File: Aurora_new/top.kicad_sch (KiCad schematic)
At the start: 27 parts, among them J17 Screw_Terminal_01x02, J18 Screw_Terminal_01x04, J19 TSW-104-27-G-D, J20 TSW-104-27-G-D, J21 XT60-M, J26 Screw_Terminal_01x08, J27 Screw_Terminal_01x08, J28 Screw_Terminal_01x03, J29 Screw_Terminal_01x03, J30 Screw_Terminal_01x03, J31 Screw_Terminal_01x03, J32 Screw_Terminal_01x03, J37 Screw_Terminal_01x03, J38 Screw_Terminal_01x03, J39 TSW-104-27-G-D, J40 XT60-M, U10 ADS1115IDGS, U11 ADS1115IDGS, U12 L7805, U8 ADS1115IDGS

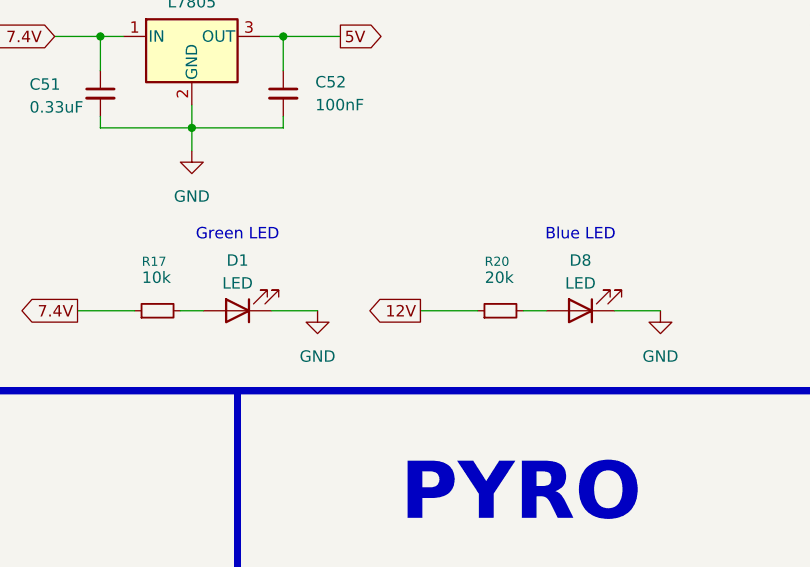
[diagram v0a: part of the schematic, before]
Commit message: bom updates (purchase links, prices, etc) and switching imu because out of stock
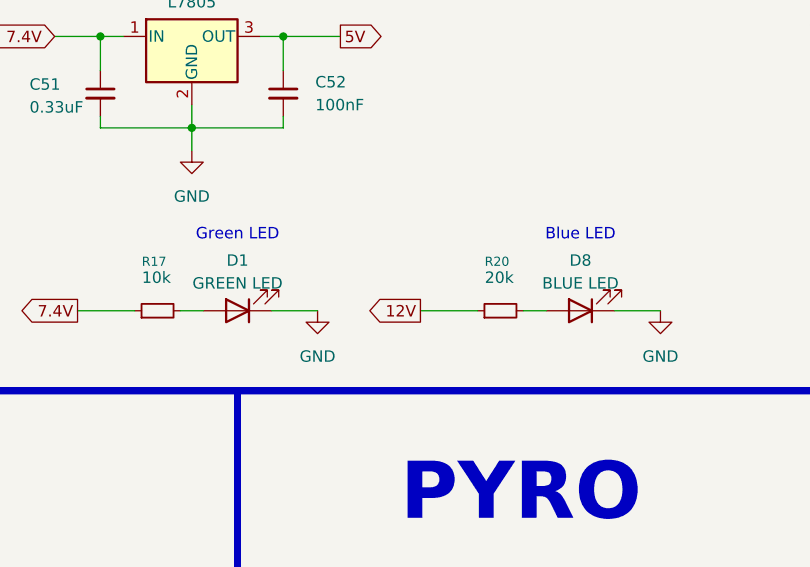
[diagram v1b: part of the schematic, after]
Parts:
- C51: PURCHASE-URL (none) -> https://www.digikey.com/en/products/detail/murata-electroni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; Price (none) -> $0.36000
- C52: PURCHASE-URL (none) -> https://www.digikey.com/en/products/detail/kyocera-avx/KGM1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; Price (none) -> $0.00700
- D1: value LED -> GREEN LED; PURCHASE-URL (none) -> https://www.digikey.com/en/products/detail/ams-osram-usa-in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; Price (none) -> $0.10200
- D8: value LED -> BLUE LED; PURCHASE-URL (none) -> https://www.digikey.com/en/products/detail/w%C3%BCrth-elekt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; Price (none) -> $0.17600
- J17: PURCHASE-URL (none) -> https://www.digikey.com/en/products/detail/phoenix-contact/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; Price (none) -> $1.33000
- J18: PURCHASE-URL (none) -> https://www.digikey.com/en/products/detail/phoenix-contact/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; Price (none) -> $2.06500
- J19, J20, J39: PURCHASE-URL (none) -> https://www.digikey.com/en/products/detail/samtec-inc/TSW-1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; Price (none) -> $1.81000
- J21, J40: PURCHASE-URL (none) -> https://www.tme.com/us/en-us/details/xt60-m/dc-power-connec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; Price (none) -> $0.602
- J26, J27: PURCHASE-URL (none) -> https://www.digikey.com/en/products/detail/phoenix-contact/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; Price (none) -> $4.07700
- J28, J29, J30, J31, J32, J37, J38: footprint (none) -> 1935174:PHOENIX_1935174; PURCHASE-URL (none) -> https://www.digikey.com/en/products/detail/phoenix-contact/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; Price (none) -> $0.74800
- R17: PURCHASE-URL (none) -> https://www.digikey.com/en/products/detail/bourns-inc/CR080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; Price (none) -> $0.00442
- R20: PURCHASE-URL (none) -> https://www.digikey.com/en/products/detail/bourns-inc/CR080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; Price (none) -> $0.00544
- U10, U11, U8: PURCHASE-URL (none) -> https://www.digikey.com/en/products/detail/texas-instrument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; Price (none) -> $5.12000
- U12: PURCHASE-URL (none) -> https://www.digikey.com/en/products/detail/stmicroelectroni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; Price (none) -> $0.50000

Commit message: added pyros, voltage booster
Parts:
- removed C51: 0.33uF, Capacitor_SMD:C_0805_2012Metric, symbol Device:C_Small
- removed C52: 100nF, Capacitor_SMD:C_0805_2012Metric, symbol Device:C_Small
- removed D8: BLUE LED, LED_SMD:LED_Cree-PLCC4_5x5mm_CW, symbol Device:LED
- removed J40: XT60-M, XT60-M:AMASS_XT60-M, symbol XT60-M:XT60-M
- removed U12: L7805, L7805:TO255P1020X450X2000-3, symbol Regulator_Linear:L7805
- added C62, C68: 22uf, Capacitor_SMD:C_0805_2012Metric, symbol Device:C_Small
- added C63, C67: 100nf, Capacitor_SMD:C_0805_2012Metric, symbol Device:C_Small
- added C64: 4.7uf, Capacitor_SMD:C_0805_2012Metric, symbol Device:C_Small
- added C65: 47pf, Capacitor_SMD:C_0805_2012Metric, symbol Device:C_Small
- added C66: 680pf, Capacitor_SMD:C_0805_2012Metric, symbol Device:C_Small
- added C69: 10uF, Capacitor_SMD:C_0805_2012Metric, symbol Device:C_Small
- added C70: 1uF, Capacitor_SMD:C_0805_2012Metric, symbol Device:C_Small
- added C71: 47uF, Capacitor_SMD:C_0805_2012Metric, symbol Device:C_Small
- added D6, D8: 1N4148W, Diode_SMD:D_SOD-123, symbol Diode:1N4148W
- added J40: Screw_Terminal_01x03, 1935174:PHOENIX_1935174, symbol Connector:Screw_Terminal_01x03
- added J42, J43: Screw_Terminal_01x04, footprints6:CONN_1715747_PXC, symbol Connector:Screw_Terminal_01x04
- added J44, J45, J46: Screw_Terminal_01x02, footprints5:CONN_1729128_PXC, symbol Connector:Screw_Terminal_01x02
- added L1: 2.2uH, symbol Device:L
- added Q1, Q2, Q5, Q6: AO3400A, Package_TO_SOT_SMD:SOT-23, symbol Transistor_FET:AO3400A
- added Q3, Q4, Q7, Q8: AO3401A, Package_TO_SOT_SMD:SOT-23, symbol Transistor_FET:AO3401A
- added R19: 23.7k, Resistor_SMD:R_0805_2012Metric, symbol Device:R_Small
- added R22: 100k, Resistor_SMD:R_0805_2012Metric, symbol Device:R_Small
- added R23: 1.07M, Resistor_SMD:R_0805_2012Metric, symbol Device:R_Small
- added R24: 120k, Resistor_SMD:R_0805_2012Metric, symbol Device:R_Small
- added R25, R26, R31, R32: 10k, Resistor_SMD:R_0805_2012Metric, symbol Device:R_Small
- added R27, R28, R29, R30, R33, R34: 1k, Resistor_SMD:R_0805_2012Metric, symbol Device:R_Small
- added U21: TPS61089, Package_DFN_QFN:Texas_VQFN-RNR0011A-11, symbol Regulator_Switching:TPS61089
- added U22: TPS7A4701xRGW, Package_DFN_QFN:Texas_RGW0020A_VQFN-20-1EP_5x5mm_P0.65mm_EP3.15x3.15mm, symbol Regulator_Linear:TPS7A4701xRGW
- J21: PURCHASE-URL https://www.tme.com/us/en-us/details/xt60-m/dc-power-connec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 -> https://www.digikey.com/en/products/detail/dfrobot/FIT0587/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; Price $0.602 -> 1.5
- R17: value 10k -> 1.3k
- R20: value 20k -> 374k; PURCHASE-URL https://www.digikey.com/en/products/detail/bourns-inc/CR080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 -> (none); Price $0.00544 -> $0.00442
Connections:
- net HDR_GPIO1 is gone; now on net PYRO1_CONT: J39.01
- net HDR_GPIO2 is gone; now on net PYRO2_CONT: J39.02
- net 12V: now also C68.1, Q3.2 (S), Q4.2 (S), R23.2, R25.1, R26.1, U21.6 (VOUT); no longer R20.1
- net 5V: now also C71.1, J42.1 (Pin_1), U22.1 (OUT), U22.20 (OUT)
- net 7.4V: now also C62.1, C63.1, C69.1, J40.2 (Pin_2), L1.1, Q7.2 (S), Q8.2 (S), R31.1, R32.1, U21.9 (VIN), U22.13 (EN), U22.15 (IN), U22.16 (IN)
- net ADC1_SCL: now also U11.10 (SCL)
- net ADC1_SDA: now also U11.1 (ADDR), U11.9 (SDA)
- net ADC3_IN0: now also J43.1 (Pin_1)
- net ADC3_IN1: now also J43.2 (Pin_2)
- net ADC3_IN2: now also J43.3 (Pin_3)
- net ADC3_IN3: now also J43.4 (Pin_4)
- net GND: now also R20.1, C62.2, C63.2, C64.2, C65.2, C66.2, C68.2, C69.2, C70.2, C71.2, J40.3 (Pin_3), J42.4 (Pin_4), J44.2 (Pin_2), J45.2 (Pin_2), J46.2 (Pin_2), Q1.2 (S), Q2.2 (S), Q5.2 (S), Q6.2 (S), R24.1, U21.5 (GND), U22.10 (0.4V), U22.6 (3.2V), U22.7 (GND); no longer U11.1 (ADDR)
- net PYRO1_CONT: now also R33.2; no longer U10.4 (AIN0)
- net PYRO1_GPIO: now also R29.2
- net PYRO2_CONT: now also R34.2; no longer U10.5 (AIN1)
- net PYRO2_GPIO: now also R30.2
- net SLN_1: now also R28.2
- net SLN_2: now also R27.2
- net SPKG: now also J40.1 (Pin_1)
- net at R20.2: now also U21.8 (ILIM)
- net ADC2_SCL renamed TEMP_SCL
- net TEMP_SCL: now also J42.2 (Pin_2); no longer U11.9 (SDA)
- net ADC2_SDA renamed TEMP_SDA
- net TEMP_SDA: now also J42.3 (Pin_3); no longer U11.10 (SCL)
- new net: Q6.1 (G), R30.1
- new net: Q6.3 (D), Q8.1 (G), R32.2
- new net: C66.1, R19.1
- new net: C65.1, R19.2, U21.4 (COMP)
- new net: C67.1, U21.10 (BOOT)
- new net: C67.2, L1.2, R22.2, U21.11 (SW)
- new net: Q1.1 (G), R28.1
- new net: D8.1 (K), J46.1 (Pin_1), Q8.3 (D)
- new net: R22.1, U21.1 (FSW)
- new net: Q1.3 (D), Q3.1 (G), R25.2
- new net: Q2.1 (G), R27.1
- new net: Q2.3 (D), Q4.1 (G), R26.2
- new net: D6.1 (K), J44.1 (Pin_1), Q7.3 (D)
- new net: R23.1, R24.2, U21.3 (FB)
- new net: C64.1, U21.2 (VCC), U21.7 (EN)
- new net: C70.1, U22.14 (NR)
- new net: Q5.1 (G), R29.1
- new net: Q5.3 (D), Q7.1 (G), R31.2
- new net: J45.1 (Pin_1), Q3.3 (D), Q4.3 (D)
- new net PYRO1_CONT_READ: D6.2 (A), R33.1, U10.4 (AIN0)
- new net PYRO2_CONT_READ: D8.2 (A), R34.1, U10.5 (AIN1)
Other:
- note added: "---Continuity--- The continuity check works by the microcontroller sending a 3.3v GPIO HIGH which gets current limited by the 1k resistor and then if the ematch is connected it basically looks like a short circuit or a ground from diode cathode side so simplifies the ciruit to: 3.3v GPIO - 1k - ADC_CONT - Diode -GND the ADC will read just the forward bias of the diode (~0.7v) as the rest of the v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"
- note added: "7.4 to 12v 0.5A Booster"
- note added: "TEMP Sensor Breakout Connection"
- note added: "The 3.3 GPIO is connected to the gate of N-Channel AO3400A with 1k current limiting resistor 3.3/1k = 3.3ma pulled from microncontroller GPIO when high it opens and connects the ground to the gate of the P-Channel AO3401A which creates a Vgs difference from the 12 source opening the mosfet and powering the solenoid the 10k pullup keeps that P-Channel Mosfet closed with Vgs = 0"
- note added: "The 3.3 GPIO is connected to the gate of N-Channel AO3400A with 1k current limiting resistor 3.3/1k = 3.3ma pulled from microncontroller GPIO when high it opens and connects the ground to the gate of the P-Channel AO3401A which creates a Vgs difference from the 12 source opening the mosfet and powering the solenoid the 10k pullup keeps that P-Channel Mosfet closed with Vgs = 0. When 12v is output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"
- note removed: "Add redundant mosfets for powering solenoid"
- note removed: "Blue LED"
- note removed: "Check works with 3.3v logic (may need 5v booster)"
- moved on the sheet: D1, D7, J17, J18, R17

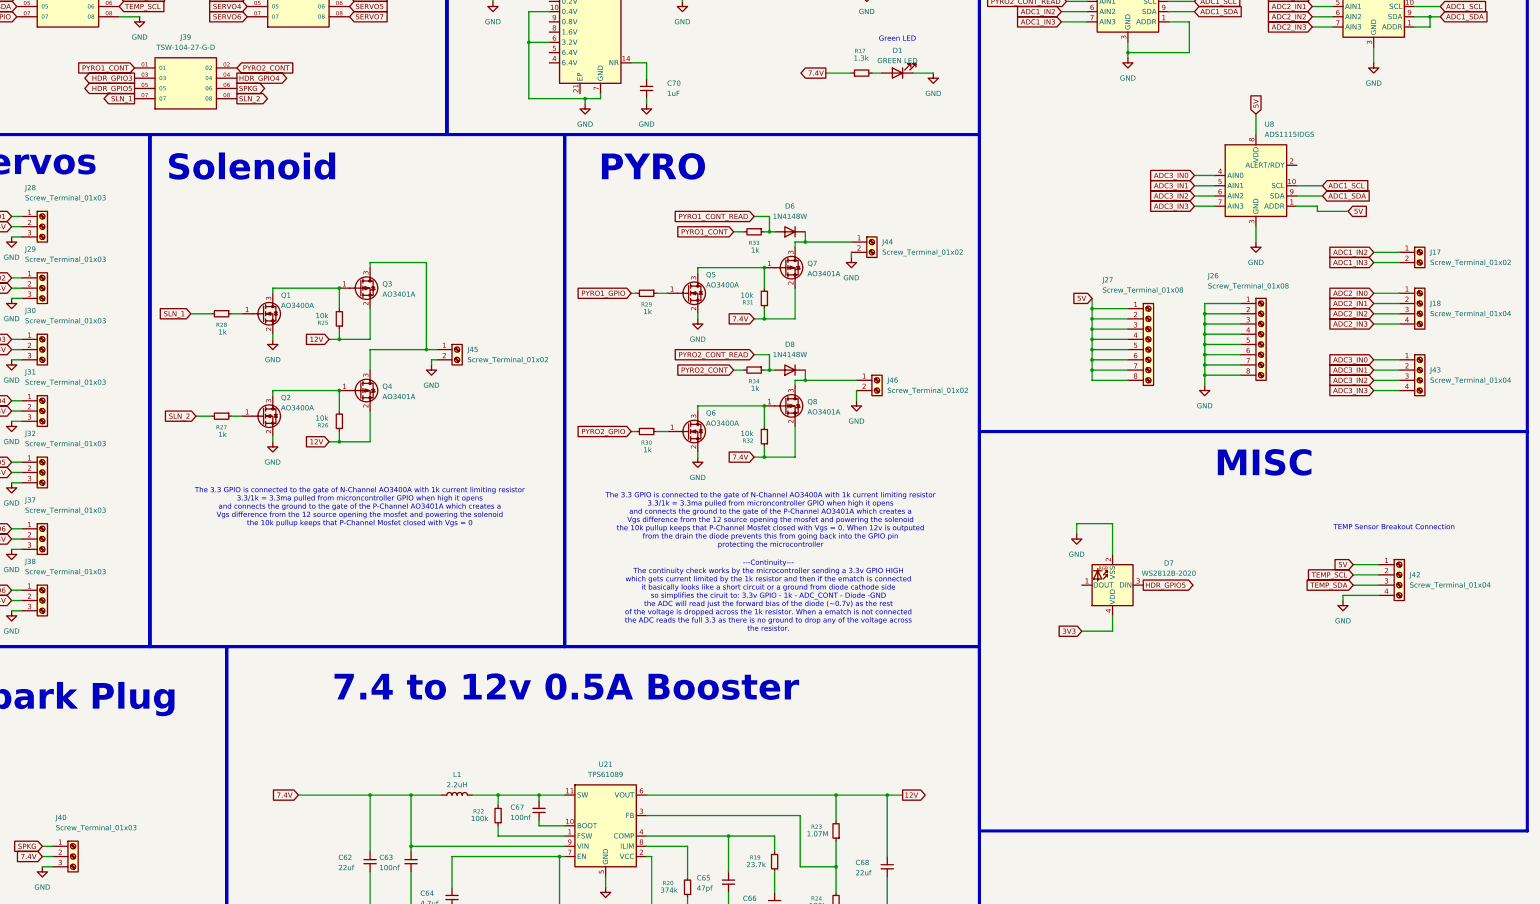
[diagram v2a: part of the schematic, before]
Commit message: working though GPIOs/CSs, Xref with cubeMX
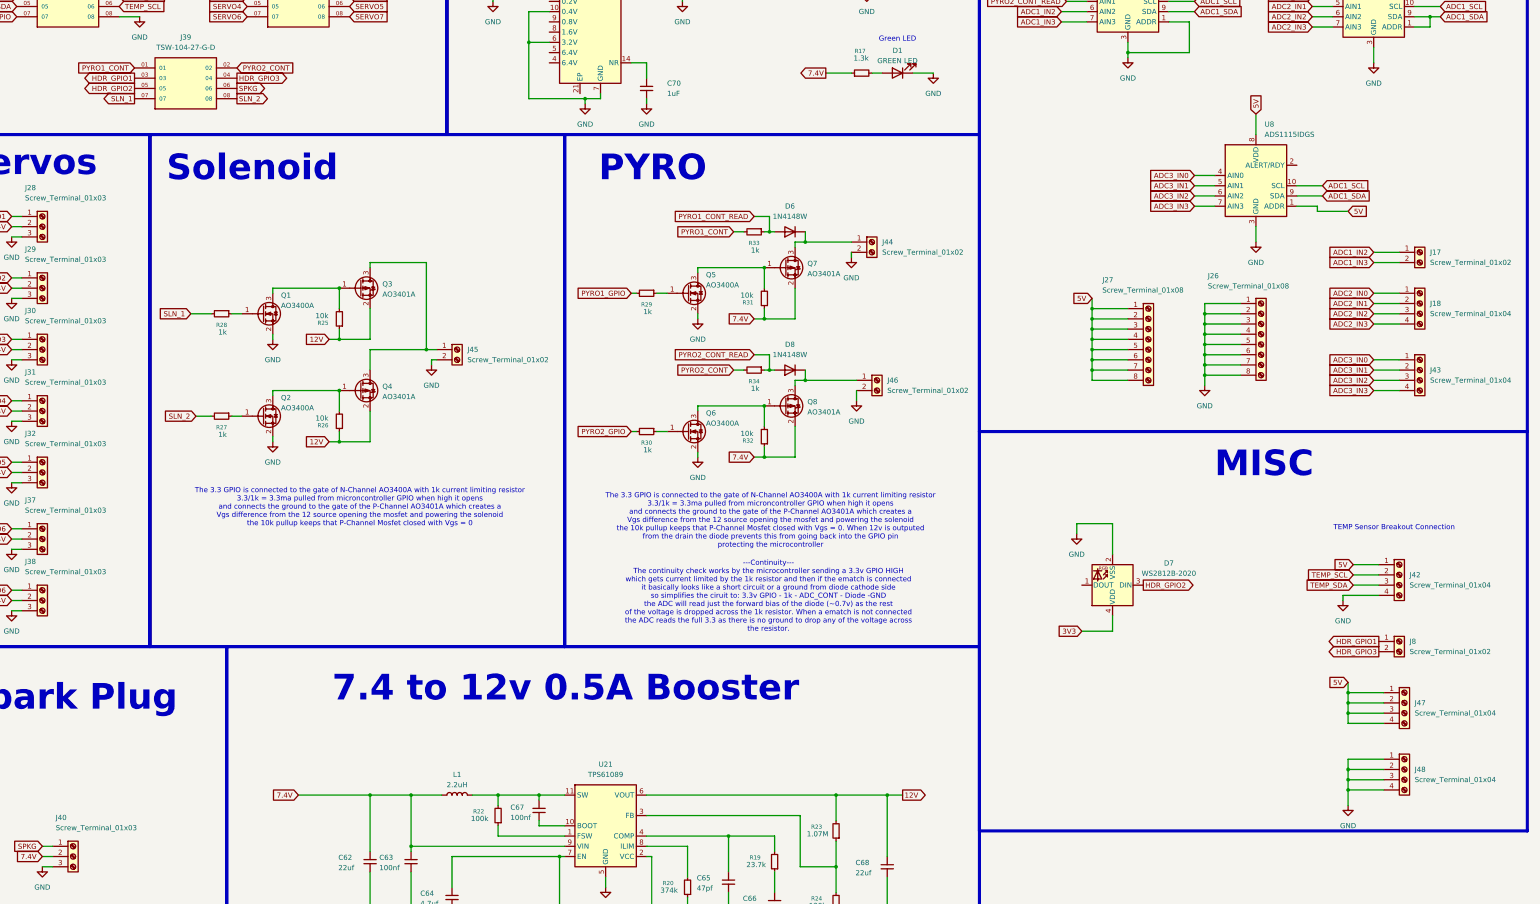
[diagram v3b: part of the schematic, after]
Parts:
- added J47, J48: Screw_Terminal_01x04, footprints6:CONN_1715747_PXC, symbol Connector:Screw_Terminal_01x04
- added J8: Screw_Terminal_01x02, footprints5:CONN_1729128_PXC, symbol Connector:Screw_Terminal_01x02
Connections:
- net HDR_GPIO4 is gone; now on net HDR_GPIO3: J39.04
- net 5V: now also J47.1 (Pin_1), J47.2 (Pin_2), J47.3 (Pin_3), J47.4 (Pin_4)
- net GND: now also J48.1 (Pin_1), J48.2 (Pin_2), J48.3 (Pin_3), J48.4 (Pin_4)
- net HDR_GPIO3: now also J8.2 (Pin_2); no longer J39.03
- net HDR_GPIO5 renamed HDR_GPIO2
- new net HDR_GPIO1: J39.03, J8.1 (Pin_1)

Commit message: changes to net labelling
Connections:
- no-connect marks 0 -> 12
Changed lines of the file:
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@@
 		(color 0 0 0 0)
 	)
+	(no_connect
+		(at 165.1 35.56)
+	)
+	(no_connect
+		(at 165.1 43.18)
+	)
+	(no_connect
+		(at 350.52 78.74)
+	)
+	(no_connect
+		(at 185.42 33.02)
+	)
+	(no_connect
+		(at 165.1 53.34)
+	)
+	(no_connect
+		(at 172.72 60.96)
+	)
+	(no_connect
+		(at 165.1 50.8)
+	)
+	(no_connect
+		(at 165.1 45.72)
+	)
+	(no_connect
+		(at 379.73 34.29)
+	)
+	(no_connect
+		(at 165.1 38.1)
+	)
+	(no_connect
+		(at 318.77 33.02)
+	)
+	(no_connect
+		(at 297.18 182.88)
+	)
 	(wire
 		(pts
@@
 	)
 	(global_label "SERVO4"
-		(shape input)
+		(shape output)
 		(at 90.17 39.37 180)
 		(fields_autoplaced yes)
@@
 	)
 	(global_label "5V"
-		(shape input)
+		(shape output)
 		(at 64.77 34.29 0)
 		(fields_autoplaced yes)
@@
 	)
 	(global_label "SERVO6"
-		(shape input)
+		(shape output)
 		(at 90.17 41.91 180)
 		(fields_autoplaced yes)
@@
 	)
 	(global_label "SERVO3"
-		(shape input)
+		(shape output)
 		(at 115.57 36.83 0)
 		(fields_autoplaced yes)
@@
 	)
 	(global_label "7.4V"
-		(shape input)
+		(shape output)
 		(at 83.82 34.29 180)
 		(fields_autoplaced yes)
@@
 	)
 	(global_label "SERVO7"
-		(shape input)
+		(shape output)
 		(at 115.57 41.91 0)
 		(fields_autoplaced yes)
@@
 	)
 	(global_label "PYRO1_GPIO"
-		(shape input)
+		(shape output)
 		(at 33.02 34.29 180)
 		(fields_autoplaced yes)
@@
 	)
 	(global_label "SERVO2"
-		(shape input)
+		(shape output)
 		(at 90.17 36.83 180)
 		(fields_autoplaced yes)
@@
 	)
 	(global_label "SERVO1"
-		(shape input)
+		(shape output)
 		(at 115.57 34.29 0)
 		(fields_autoplaced yes)
@@
 	)
 	(global_label "SERVO5"
-		(shape input)
+		(shape output)
 		(at 115.57 39.37 0)
 		(fields_autoplaced yes)
@@
 	)
 	(global_label "PYRO2_GPIO"
-		(shape input)
+		(shape output)
 		(at 33.02 41.91 180)
 		(fields_autoplaced yes)
